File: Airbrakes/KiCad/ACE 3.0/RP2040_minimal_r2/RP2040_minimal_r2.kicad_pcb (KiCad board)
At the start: 2 copper layers, 52 x 51 mm, 47 parts, among them J1 USB_B_Micro, J2 Conn_01x02, J3 104031-0811, J4 Conn_02x18_Odd_Even, U1 NCP1117-3.3_SOT223, U2 W25Q128JVS, U3 RP2040, U4 BMI088, U5 BMP581, U6 BMM350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

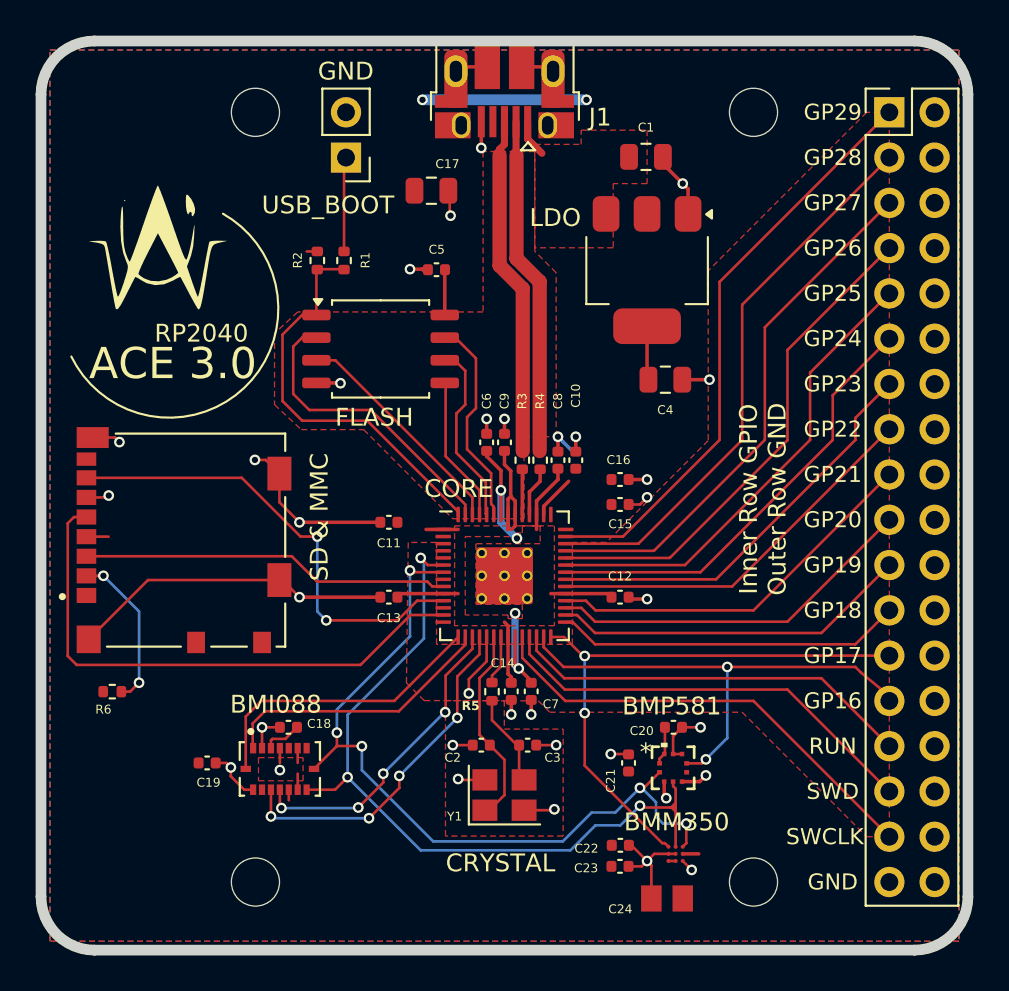
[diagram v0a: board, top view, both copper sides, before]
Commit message: DRC warning fixes
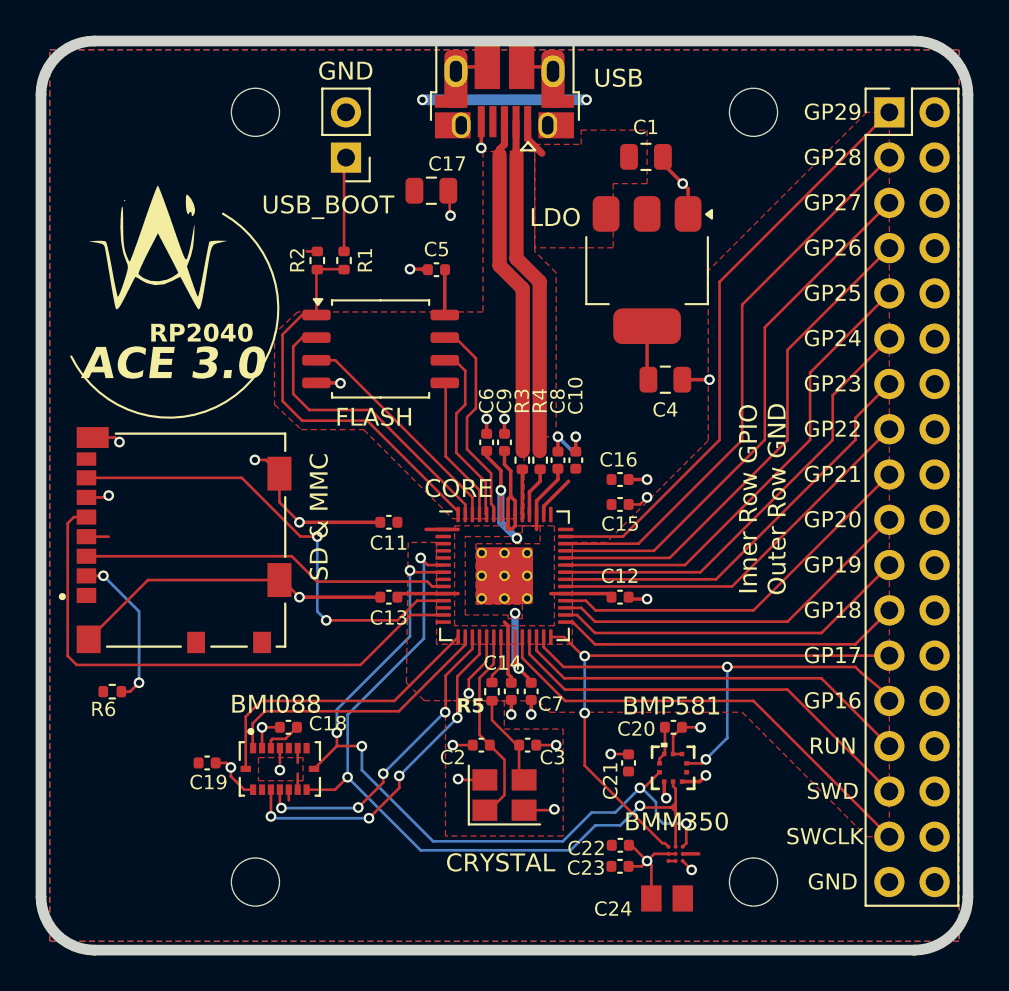
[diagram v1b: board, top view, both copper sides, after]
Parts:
- renumbered J1 to USB

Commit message: Update footprint refs
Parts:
- R6: value R -> 10k
- renumbered USB to J1
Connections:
- U5 pad 6: +3V3 -> unconnected-(U5-CSB-Pad6)
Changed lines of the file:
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@@
 	(net 58 "/SCLK")
 	(net 59 "/GPIO9")
+	(net 60 "unconnected-(U5-CSB-Pad6)")
 	(footprint "Capacitor_SMD:C_0805_2012Metric"
 		(layer "F.Cu")
@@
 		(descr "Micro USB Type B 10103594-0001LF, http://cdn.amphenol-icc.com/media/wysiwyg/files/drawing/10103594.pdf")
 		(tags "USB USB_B USB_micro USB_OTG")
-		(property "Reference" "USB"
+		(property "Reference" "J1"
 			(at -6.4 -0.4 180)
 			(layer "F.SilkS")
+			(hide yes)
 			(effects
 				(font
@@
 			(net 41 "unconnected-(U4-CSB2-Pad5)")
 			(pinfunction "CSB2")
-			(pintype "input")
+			(pintype "input+no_connect")
 			(solder_mask_margin 0.102)
 		)
@@
 			(net 42 "unconnected-(U4-CSB1-Pad14)")
 			(pinfunction "CSB1")
-			(pintype "input")
+			(pintype "input+no_connect")
 			(solder_mask_margin 0.102)
 		)
@@
 			)
 		)
-		(property "Value" "R"
+		(property "Value" "10k"
 			(at 0 1.17 0)
 			(layer "F.Fab")
@@
 			)
 		)
-		(property "Footprint" "BGA9_BMM350_BOS"
+		(property "Footprint" "BMM350:BGA9_BMM350_BOS"
 			(at 0 0 0)
 			(unlocked yes)
@@
 			)
 		)
-		(property "Footprint" "QFN10_BMP581_BOS"
+		(property "Footprint" "BMP581:QFN10_BMP581_BOS"
 			(at 0 0 0)
 			(unlocked yes)
@@
 			(size 0.254 0.2794)
 			(layers "F.Cu" "F.Paste" "F.Mask")
-			(net 5 "+3V3")
+			(net 60 "unconnected-(U5-CSB-Pad6)")
 			(pinfunction "CSB")
-			(pintype "unspecified")
+			(pintype "unspecified+no_connect")
 		)
 		(pad "7" smd rect

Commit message: buttons
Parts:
- removed J2: Conn_01x02, Connector_PinHeader_2.54mm:PinHeader_1x02_P2.54mm_Vertical
- added U7: B3U-1000P, Button_Switch_SMD:SW_SPST_B3U-1000P, F.Cu at (91.1, 75.5)
- added U8: B3U-1000P, Button_Switch_SMD:SW_SPST_B3U-1000P, F.Cu at (79.9, 75.1)
- moved C12 2.54 mm to (109.0, 101.2)
- moved G*** 1.60 mm to (80.8, 83.3)
- moved C17 0.82 mm to (96.1, 77.6)
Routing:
- net /RUN: track 22.8 -> 74.7 mm, vias 0 -> 2
- net +3V3: track 45.1 -> 47.7 mm
- net /~{USB_BOOT}: track 5.34 -> 4.61 mm

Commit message: Final review + DRC pass
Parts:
- moved C22 4.66 mm to (111.0, 113.9), turned to 90 degrees
- moved C13 1.68 mm to (93.0, 99.6)
- moved C20 0.48 mm to (109.0, 108.6)
- moved U6 0.47 mm to (109.1, 115.5)
- moved U5 0.46 mm to (109.0, 110.8)
- moved C21 0.46 mm to (106.5, 110.5)
- moved C18 0.41 mm to (87.8, 108.1)
- moved C24 0.37 mm to (109.3, 118.4), turned to 90 degrees
- moved C23 0.36 mm to (106.8, 116.3), turned to 180 degrees
- moved U8 0.35 mm to (79.9, 75.5)
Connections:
- C24 pad 2: +3V3 -> /CRST
- U3 pad 14: /GPIO11 -> /MOSI
- U3 pad 9: /MOSI -> /GPIO7
- U6 pad C2: +3V3 -> /CRST
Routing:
- net GND: track 84.7 -> 63.8 mm, vias 34 -> 39
- net /SCLK: track 31.1 -> 22.3 mm
- net /MISO: track 26.2 -> 23.0 mm, vias 2 -> 0
- net +3V3: track 47.7 -> 45.3 mm, vias 2 -> 4
- net /CRST: track 0.00 -> 2.18 mm
- net /SDA: track 43.9 -> 41.8 mm
- net /MOSI: track 20.7 -> 21.7 mm
- net /SCL: track 43.3 -> 43.1 mm, vias 5 -> 4
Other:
- board text added: "BOOT"
- board text removed: "USB_BOOT"

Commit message: silkscreeen....
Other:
- board text added: "R.I.P ACE 1.0"
- board text added: "{dblquote}I-Is that the aft?{dblquote}"
- board text added: "{dblquote}LOGAN! you said it was WATERTIGHT!!{dblquote}"
- board text added: "{dblquote}May the wind upon this ACE streak along with such a grace as to fly high but true, 5120 beyond, toward that sky everblue.{dblquote}"
- board text added: "{dblquote}William, you talk too much!{dblquote}"
- board text added: "{dblquote}continuity means that there exists continuity..{dblquote}"
- board text added: "{dblquote}it'll take only 30 min{dblquote}"
- board text added: "{dblquote}it's got one more flight in it{dblquote}"
- board text added: "{dblquote}just yappin'{dblquote}"
- board text added: "{dblquote}mack stinks{dblquote} (—leela)"
- board text added: "{dblquote}no, i've got gasoline{dblquote}"
- board text added: "{dblquote}unbelievable{dblquote}"
- board text added: "{dblquote}vibes-based engineering{dblquote}"
- board text added: "{dblquote}yo, you gotta lock IN{dblquote}"
- board text removed: "—{dblquote}Per Aspera Ad Astra{dblquote}"
